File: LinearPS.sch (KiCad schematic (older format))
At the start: 91 parts, among them J1 Conn_01x03, J2 Conn_01x02, J3 Conn_01x03, J4 Conn_01x01, J5 Conn_01x01, J6 Conn_01x01, J7 Conn_01x01, J8 Conn_01x02, Q1 2N3904, Q2 TIP41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

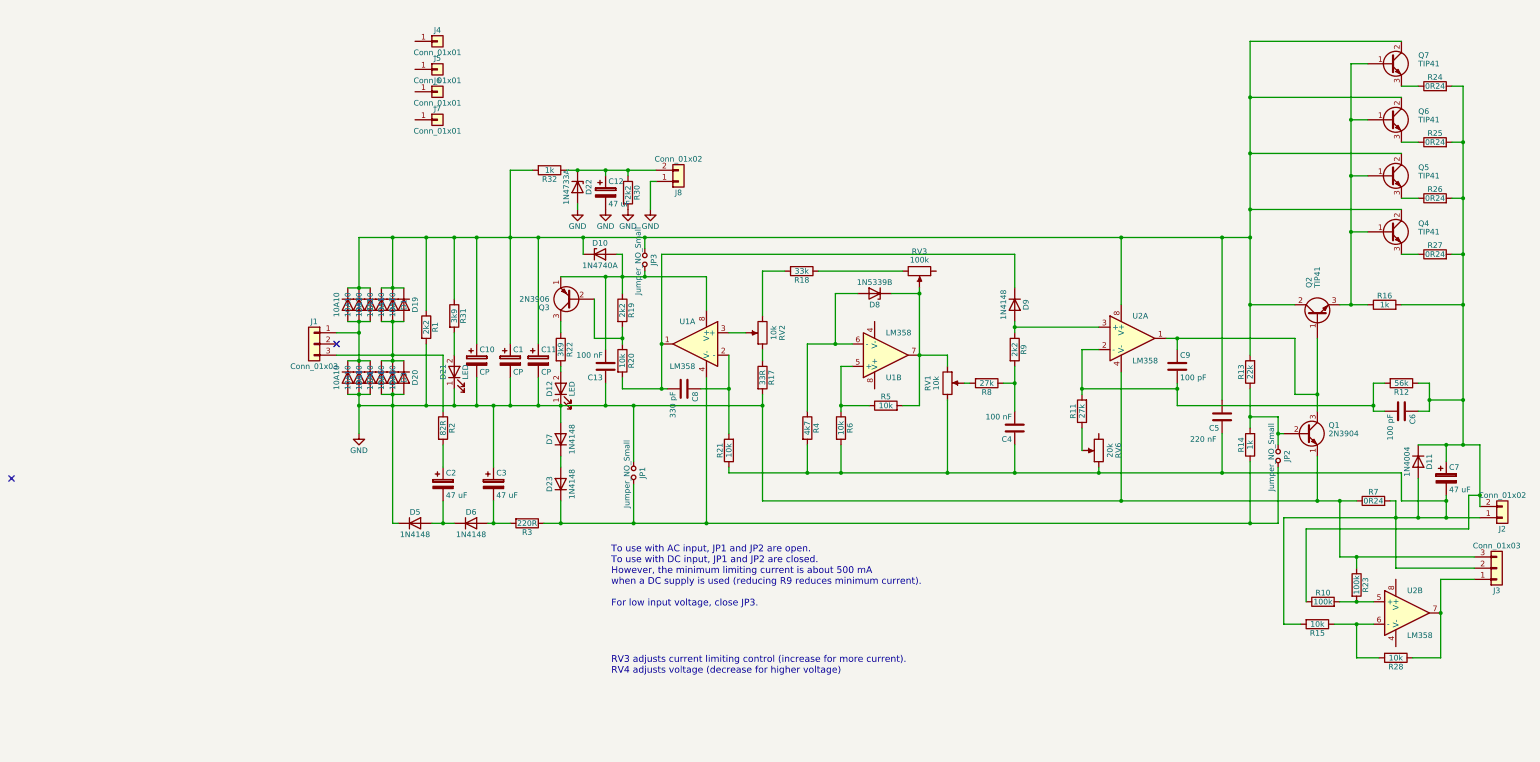
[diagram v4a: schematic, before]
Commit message: Added external control input for current and voltage
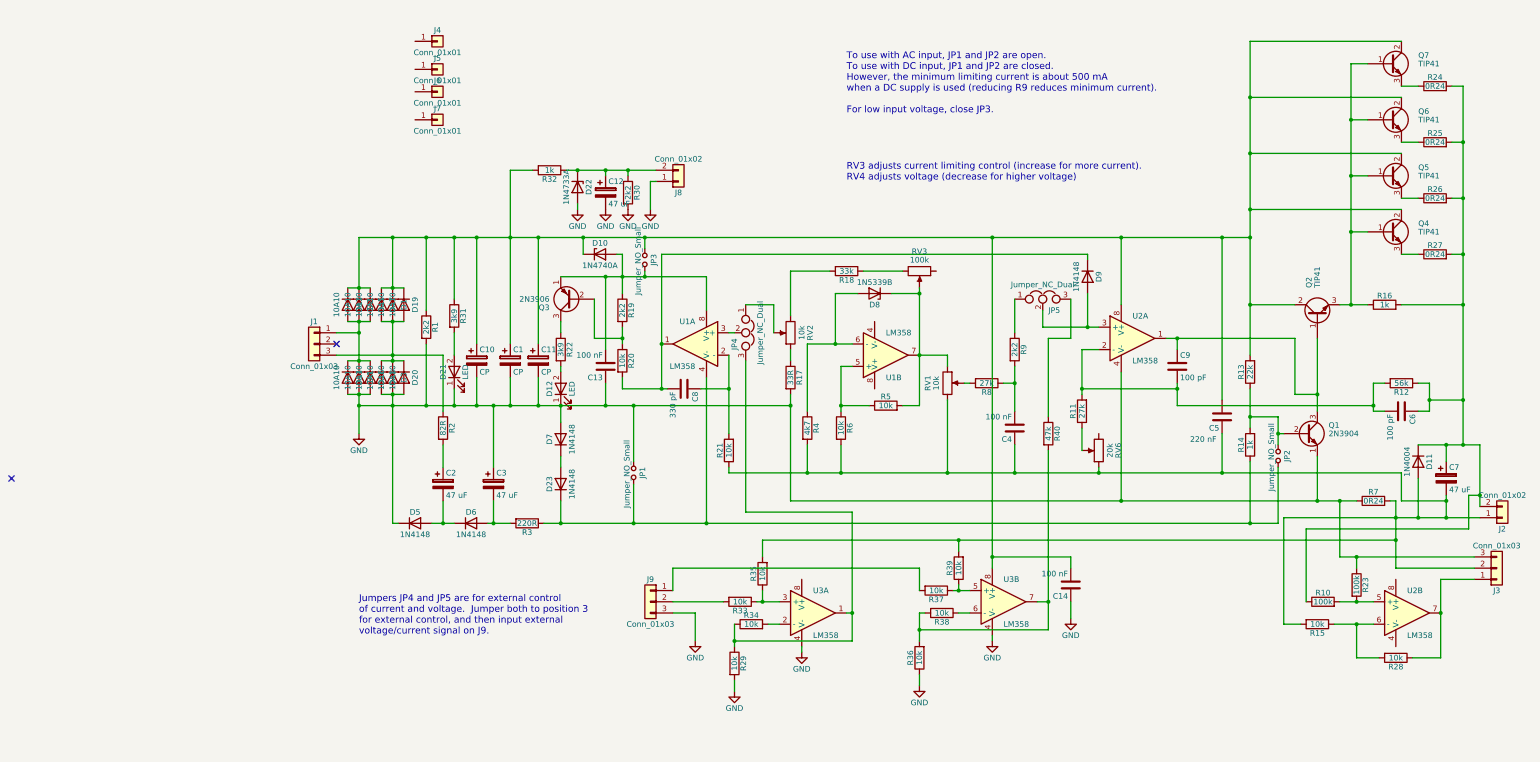
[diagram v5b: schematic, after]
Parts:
- added C14: 100 nF, Capacitors_THT:C_Disc_D5.0mm_W2.5mm_P5.00mm, symbol C
- added J9: Conn_01x03, Connectors_Molex:Molex_KK-6410-03_03x2.54mm_Straight, symbol Conn_01x03
- added JP4, JP5: Jumper_NC_Dual, Pin_Headers:Pin_Header_Straight_1x03_Pitch2.54mm, symbol Jumper_NC_Dual
- added R29, R33, R34, R35, R36, R37, R38, R39: 10k, Resistors_THT:R_Axial_DIN0207_L6.3mm_D2.5mm_P7.62mm_Horizontal, symbol R
- added R40: 47k, Resistors_THT:R_Axial_DIN0207_L6.3mm_D2.5mm_P7.62mm_Horizontal, symbol R
- added U3: LM358, Housings_DIP:DIP-8_W7.62mm_Socket, symbol LM358
- J3: footprint Connectors_Terminal_Blocks:TerminalBlock_bornier-3_P5.08mm -> Connectors_Molex:Molex_KK-6410-03_03x2.54mm_Straight
- J8: footprint Connectors_Terminal_Blocks:TerminalBlock_bornier-2_P5.08mm -> Connectors_Molex:Molex_KK-6410-02_02x2.54mm_Straight
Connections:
- net GND: now also C14.1, J9.3 (Pin_3), R29.2, R36.1, U3.4 (V-), U3.4 (V-)
- net at C1.1, C10.1, C11.1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: now also C14.2, U3.8 (V+)
- net at C4.1, C5.1, C7.2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: now also R35.2, R39.2
- net at U1.3 (+): now also JP4.2; no longer RV2.2
- net at D9.2 (A), U2.3 (+): now also JP5.2; no longer R9.1
- new net: JP4.1, RV2.2
- new net: JP5.1, R9.1
- new net: JP4.3, R29.1, R34.1, U3.1
- new net: R34.2, U3.2 (-)
- new net: R33.1, R35.1, U3.3 (+)
- new net: R37.1, R39.1, U3.5 (+)
- new net: R38.1, U3.6 (-)
- new net: R36.2, R38.2, R40.2, U3.7
- new net: J9.1 (Pin_1), R37.2
- new net: J9.2 (Pin_2), R33.2
- new net: JP5.3, R40.1
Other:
- note added: "Jumpers JP4 and JP5 are for external control\nof current and voltage. Jumper both to position 3\nfor external control, and then input external\nvoltage/current signal on J9."
- moved on the sheet: D9, R17, R18, RV2

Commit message: Fixed stupid mistake in external input
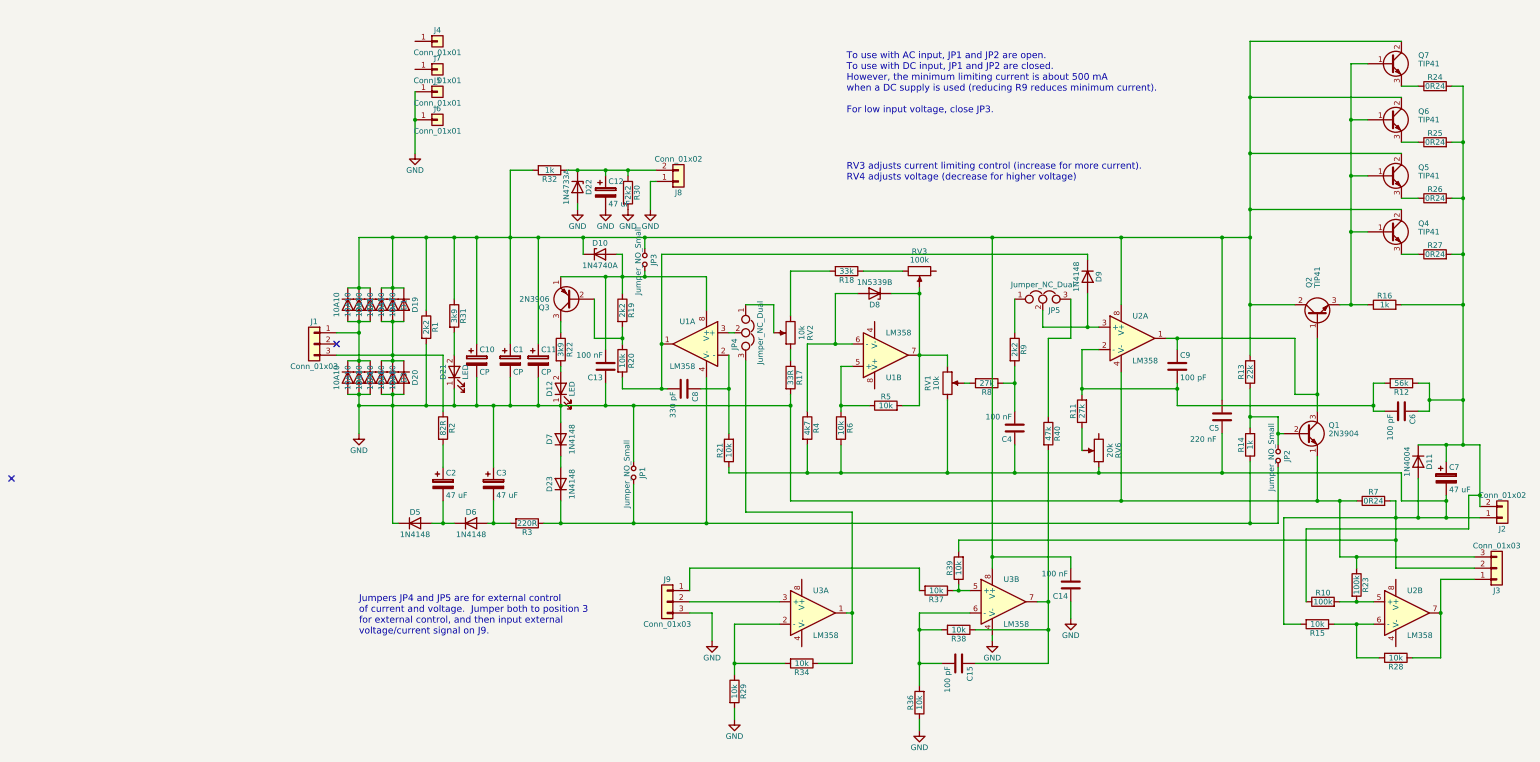
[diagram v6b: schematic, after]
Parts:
- removed R33, R35: 10k, Resistors_THT:R_Axial_DIN0207_L6.3mm_D2.5mm_P7.62mm_Horizontal, symbol R
- added C15: 100 pF, Capacitors_THT:C_Disc_D5.0mm_W2.5mm_P5.00mm, symbol C
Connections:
- net GND: now also J5.1 (Pin_1), J6.1 (Pin_1); no longer U3.4 (V-)
- net at JP4.3, R34.1, U3.1: no longer R29.1
- net at R34.2, U3.2 (-): now also R29.1
- net at U3.3 (+): now also J9.2 (Pin_2)
- net at U3.6 (-): now also R36.2, R38.2, C15.2; no longer R38.1
- net at R40.2, U3.7: now also R38.1, C15.1; no longer R36.2, R38.2
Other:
- moved on the sheet: J5, J6, J7, J9, R29, R34, R36, R38

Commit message: Cleaned up schematic to make it easier to read
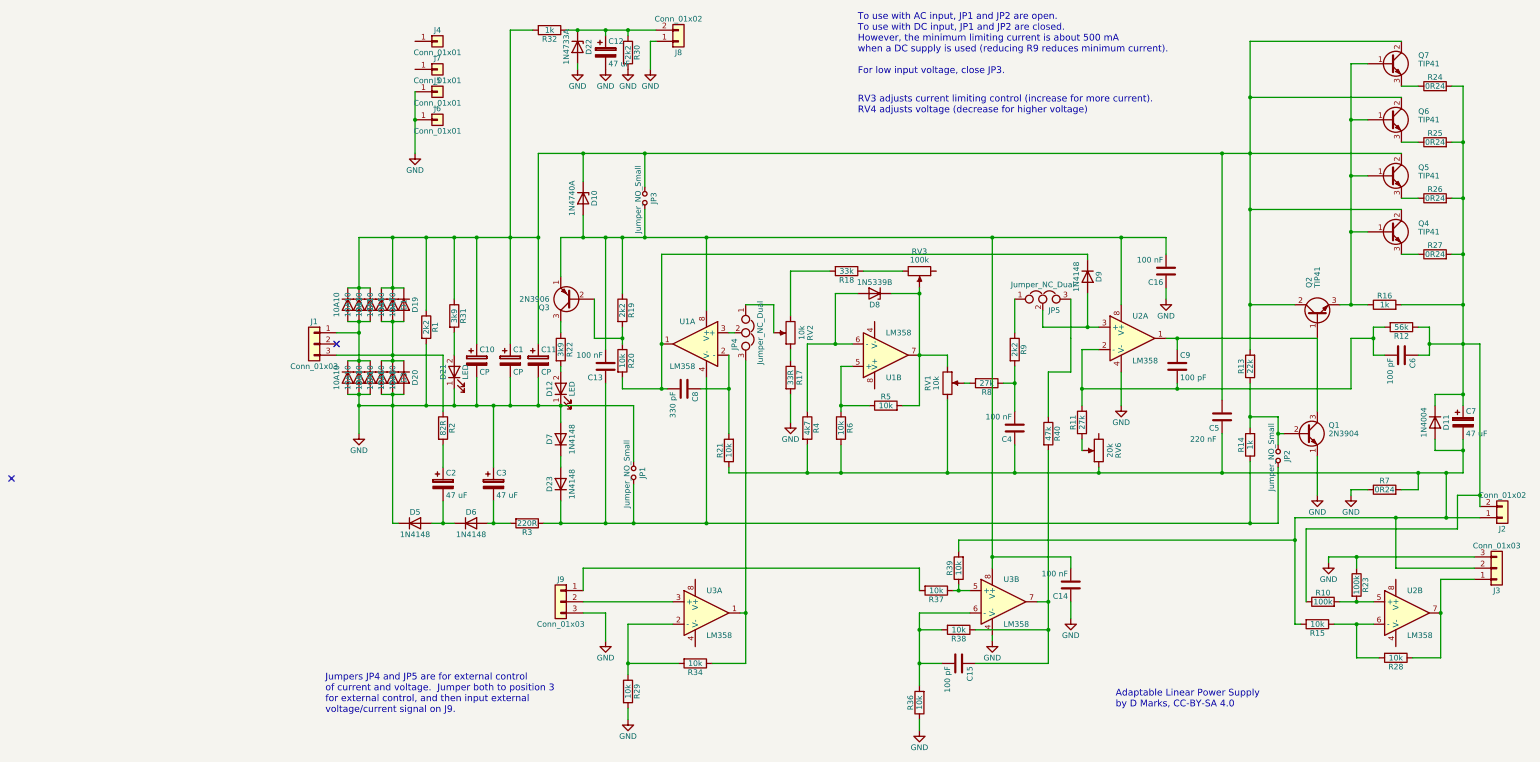
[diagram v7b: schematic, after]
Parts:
- added C16: 100 nF, Capacitors_THT:C_Disc_D5.0mm_W2.5mm_P5.00mm, symbol C
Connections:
- net GND: now also C16.1; no longer C13.1
- net at C1.1, C10.1, C11.1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: no longer C14.2, U2.8 (V+), U3.8 (V+)
- net at C13.2, D10.2 (A), JP3.2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: now also C14.2, U2.8 (V+), U3.8 (V+), C16.2
- net at D23.1 (K), JP1.2, JP2.2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: now also C13.1
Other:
- note added: "Adaptable Linear Power Supply\nby D Marks, CC-BY-SA 4.0"
- moved on the sheet: C12, C6, C7, D10, D11, D22, J8, J9, JP3, R11, R12, R13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

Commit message: Modified for larger diode and capactior footprints, TO-220 and TO-247 devices
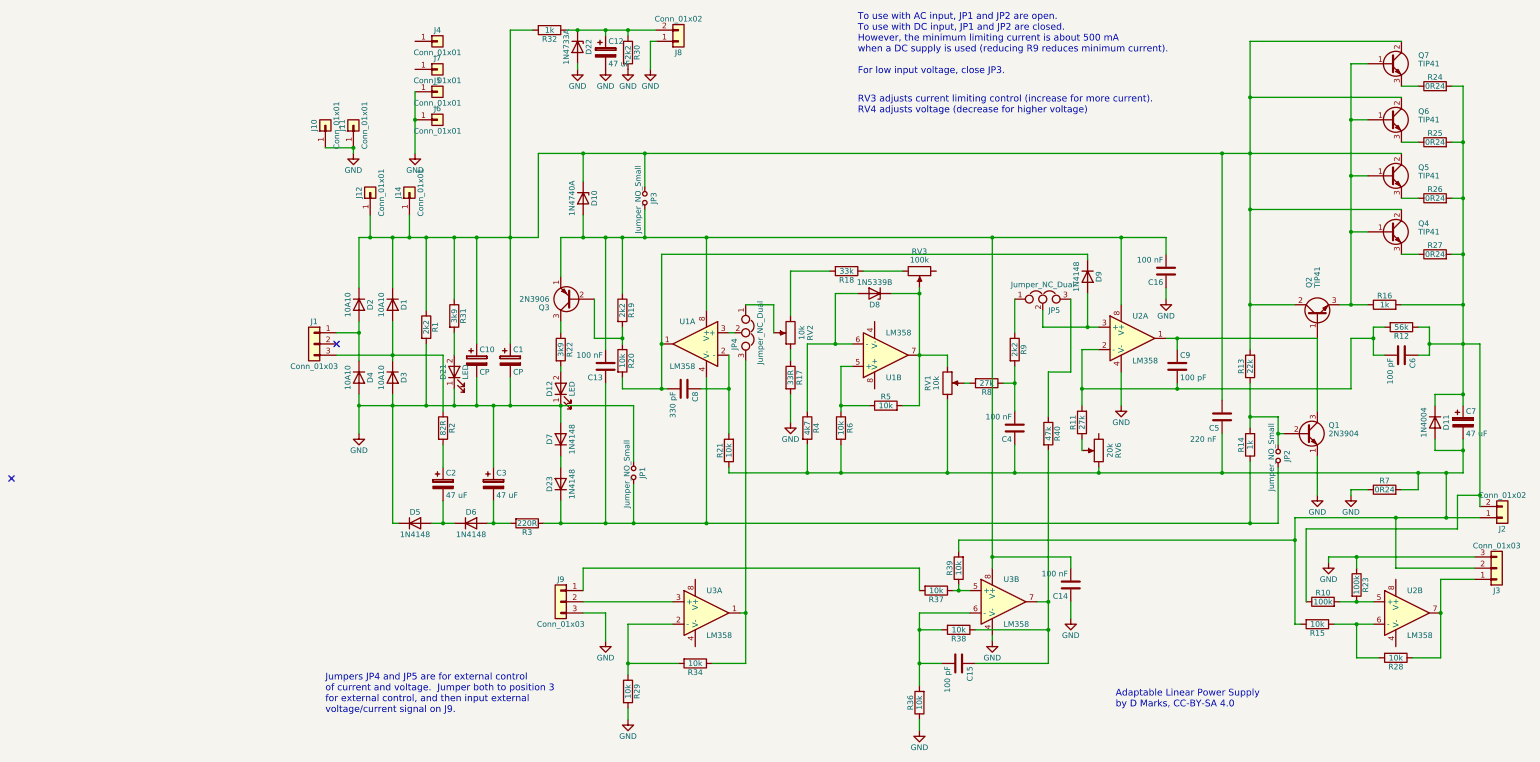
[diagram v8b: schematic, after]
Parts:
- removed C11: CP, Capacitors_THT:CP_Radial_D13.0mm_P7.50mm, symbol CP
- removed D13, D14, D15, D16, D17, D18, D19, D20: 10A10, Diodes_THT:D_DO-201_P15.24mm_Horizontal, symbol D
- added J10, J11, J12, J14: Conn_01x01, Connectors:1pin, symbol Conn_01x01
- C1, C10: footprint Capacitors_THT:CP_Radial_D13.0mm_P7.50mm -> Capacitors_THT:CP_Radial_D18.0mm_P7.50mm
- D1, D2, D3, D4: footprint Diodes_THT:D_DO-201_P15.24mm_Horizontal -> Diodes_THT:D_P600_R-6_P12.70mm_Horizontal
- Q4, Q5, Q6, Q7: footprint linearps:TO-220-3_Vertical_WithPads -> linearps:TO-220-3_Vertical_WithBigPads
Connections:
- net GND: now also J10.1 (Pin_1), J11.1 (Pin_1)
- net at C1.1, C10.1, C5.2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: now also J12.1 (Pin_1), J14.1 (Pin_1)
